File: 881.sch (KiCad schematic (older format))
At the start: 79 parts

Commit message: schematic captured, started layout
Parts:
- SW1: renamed from SW?; footprint (none) -> MyModules:SS-12F45-1P2T-SLIDE
- gave numbers to parts that had none: 78
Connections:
- wire segments 188 -> 128

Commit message: ground stitching, tweaking
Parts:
- R1, R11, R12, R13, R14, R16, R17, R18, R19, R2, R20, R3, R4, R6, R7, R8, R9: value 220 -> 1K
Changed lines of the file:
@@
 P 1775 6675
 F 0 "R1" V 1875 6675 50  0000 C CNN
-F 1 "220" V 1695 6675 50  0000 C CNN
+F 1 "1K" V 1695 6675 50  0000 C CNN
 F 2 "MyModules:SM0603-R-YAGEO" H 1775 6675 60  0001 C CNN
 F 3 "~" H 1775 6675 60  0000 C CNN
@@
 P 1775 7750
 F 0 "R2" V 1875 7750 50  0000 C CNN
-F 1 "220" V 1695 7750 50  0000 C CNN
+F 1 "1K" V 1695 7750 50  0000 C CNN
 F 2 "MyModules:SM0603-R-YAGEO" H 1775 7750 60  0001 C CNN
 F 3 "~" H 1775 7750 60  0000 C CNN
@@
 P 1775 8800
 F 0 "R3" V 1875 8800 50  0000 C CNN
-F 1 "220" V 1695 8800 50  0000 C CNN
+F 1 "1K" V 1695 8800 50  0000 C CNN
 F 2 "MyModules:SM0603-R-YAGEO" H 1775 8800 60  0001 C CNN
 F 3 "~" H 1775 8800 60  0000 C CNN
@@
 P 1775 9875
 F 0 "R4" V 1875 9875 50  0000 C CNN
-F 1 "220" V 1695 9875 50  0000 C CNN
+F 1 "1K" V 1695 9875 50  0000 C CNN
 F 2 "MyModules:SM0603-R-YAGEO" H 1775 9875 60  0001 C CNN
 F 3 "~" H 1775 9875 60  0000 C CNN
@@
 P 3675 6675
 F 0 "R6" V 3775 6675 50  0000 C CNN
-F 1 "220" V 3595 6675 50  0000 C CNN
+F 1 "1K" V 3595 6675 50  0000 C CNN
 F 2 "MyModules:SM0603-R-YAGEO" H 3675 6675 60  0001 C CNN
 F 3 "~" H 3675 6675 60  0000 C CNN
@@
 P 3675 7750
 F 0 "R7" V 3775 7750 50  0000 C CNN
-F 1 "220" V 3595 7750 50  0000 C CNN
+F 1 "1K" V 3595 7750 50  0000 C CNN
 F 2 "MyModules:SM0603-R-YAGEO" H 3675 7750 60  0001 C CNN
 F 3 "~" H 3675 7750 60  0000 C CNN
@@
 P 3675 8800
 F 0 "R8" V 3775 8800 50  0000 C CNN
-F 1 "220" V 3595 8800 50  0000 C CNN
+F 1 "1K" V 3595 8800 50  0000 C CNN
 F 2 "MyModules:SM0603-R-YAGEO" H 3675 8800 60  0001 C CNN
 F 3 "~" H 3675 8800 60  0000 C CNN
@@
 P 3675 9875
 F 0 "R9" V 3775 9875 50  0000 C CNN
-F 1 "220" V 3595 9875 50  0000 C CNN
+F 1 "1K" V 3595 9875 50  0000 C CNN
 F 2 "MyModules:SM0603-R-YAGEO" H 3675 9875 60  0001 C CNN
 F 3 "~" H 3675 9875 60  0000 C CNN
@@
 P 5550 6675
 F 0 "R11" V 5650 6675 50  0000 C CNN
-F 1 "220" V 5470 6675 50  0000 C CNN
+F 1 "1K" V 5470 6675 50  0000 C CNN
 F 2 "MyModules:SM0603-R-YAGEO" H 5550 6675 60  0001 C CNN
 F 3 "~" H 5550 6675 60  0000 C CNN
@@
 P 5550 7750
 F 0 "R12" V 5650 7750 50  0000 C CNN
-F 1 "220" V 5470 7750 50  0000 C CNN
+F 1 "1K" V 5470 7750 50  0000 C CNN
 F 2 "MyModules:SM0603-R-YAGEO" H 5550 7750 60  0001 C CNN
 F 3 "~" H 5550 7750 60  0000 C CNN
@@
 P 5550 8800
 F 0 "R13" V 5650 8800 50  0000 C CNN
-F 1 "220" V 5470 8800 50  0000 C CNN
+F 1 "1K" V 5470 8800 50  0000 C CNN
 F 2 "MyModules:SM0603-R-YAGEO" H 5550 8800 60  0001 C CNN
 F 3 "~" H 5550 8800 60  0000 C CNN
@@
 P 5550 9875
 F 0 "R14" V 5650 9875 50  0000 C CNN
-F 1 "220" V 5470 9875 50  0000 C CNN
+F 1 "1K" V 5470 9875 50  0000 C CNN
 F 2 "MyModules:SM0603-R-YAGEO" H 5550 9875 60  0001 C CNN
 F 3 "~" H 5550 9875 60  0000 C CNN
@@
 P 7775 6675
 F 0 "R16" V 7875 6675 50  0000 C CNN
-F 1 "220" V 7695 6675 50  0000 C CNN
+F 1 "1K" V 7695 6675 50  0000 C CNN
 F 2 "MyModules:SM0603-R-YAGEO" H 7775 6675 60  0001 C CNN
 F 3 "~" H 7775 6675 60  0000 C CNN
@@
 P 7775 7725
 F 0 "R17" V 7875 7725 50  0000 C CNN
-F 1 "220" V 7695 7725 50  0000 C CNN
+F 1 "1K" V 7695 7725 50  0000 C CNN
 F 2 "MyModules:SM0603-R-YAGEO" H 7775 7725 60  0001 C CNN
 F 3 "~" H 7775 7725 60  0000 C CNN
@@
 P 7775 8775
 F 0 "R18" V 7875 8775 50  0000 C CNN
-F 1 "220" V 7695 8775 50  0000 C CNN
+F 1 "1K" V 7695 8775 50  0000 C CNN
 F 2 "MyModules:SM0603-R-YAGEO" H 7775 8775 60  0001 C CNN
 F 3 "~" H 7775 8775 60  0000 C CNN
@@
 P 7775 9850
 F 0 "R19" V 7875 9850 50  0000 C CNN
-F 1 "220" V 7695 9850 50  0000 C CNN
+F 1 "1K" V 7695 9850 50  0000 C CNN
 F 2 "MyModules:SM0603-R-YAGEO" H 7775 9850 60  0001 C CNN
 F 3 "~" H 7775 9850 60  0000 C CNN
@@
 P 10125 6700
 F 0 "R20" V 10225 6700 50  0000 C CNN
-F 1 "220" V 10045 6700 50  0000 C CNN
+F 1 "1K" V 10045 6700 50  0000 C CNN
 F 2 "MyModules:SM0603-R-YAGEO" H 10125 6700 60  0001 C CNN
 F 3 "~" H 10125 6700 60  0000 C CNN

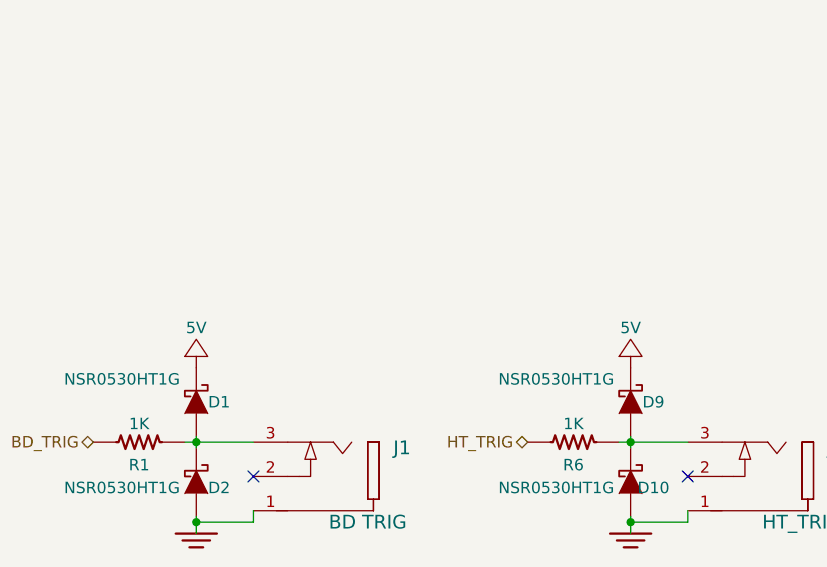
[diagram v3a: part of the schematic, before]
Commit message: notes added, going to turn this into trigger-MIDI converter
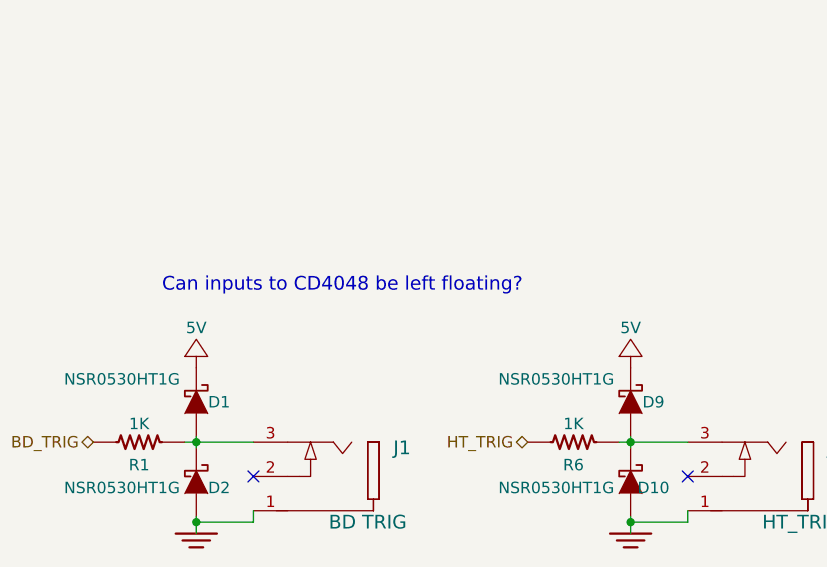
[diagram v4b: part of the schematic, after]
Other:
- note added: "Can inputs to CD4048 be left floating?"
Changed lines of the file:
@@
 	1    0    0    -1
 $EndComp
+Text Notes 1875 6025 0    60   ~ 0
+Can inputs to CD4048 be left floating?
 $EndSCHEMATC

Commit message: first version of 881, obsolete. next commit will begin with new version for connection to 880 TII and DIN EXP
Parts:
- removed C1: 0.01µ, MyModules:SM0603-C-MURATA, symbol C_US
- removed C2, C3: 0.1µ, MyModules:SM0603-C-MURATA, symbol C_US
- removed D1, D10, D11, D12, D13, D14, D15, D16, D17, D18, D19, D2, D20, D21, D22, D23, D24, D25, D26, D3, D4, D5, D6, D7, D8, D9: NSR0530HT1G, MyModules:SOD323-C1A2, symbol D_Schottky
- removed R1, R11, R12, R13, R14, R16, R2, R3, R4, R6, R7, R8, R9: 1K, MyModules:SM0603-R-YAGEO, symbol R_US
- removed R5: 22, MyModules:SM0603-R-YAGEO, symbol R_US
- removed SW1: SPDT, MyModules:SS-12F45-1P2T-SLIDE, symbol SPDT
- removed U1, U2: CD4048B, Housings_SSOP:TSSOP-16_4.4x5mm_Pitch0.65mm, symbol CD4048B
- removed X1: SYNC24 OUT, MyModules:SD-50BV-5DIN, symbol MIDI_DIN
- added C?: 1μ, MyModules:SM0603-C-JRL, symbol C_US
- added C? (x2): 47µ, Capacitors_SMD:c_elec_4x5.3, symbol CP_US
- added C? (x12): 0.1μ, MyModules:SM0603-C-JRL, symbol C_US
- added C? (x2): 24p, MyModules:SM0603-C-JRL, symbol C_US
- added C? (x5): 0.1µ, MyModules:SM0603-C-JRL, symbol C_US
- added D? (x2): SMB, MyModules:SMB-1C2A, symbol D
- added D? (x4): NSR0530HT1G, MyModules:SOD323-C1A2, symbol D_Schottky
- added D?: LED 7, MyModules:3MM-LED-C1A2, symbol LED
- added D?: LED 8, MyModules:3MM-LED-C1A2, symbol LED
- added D?: LED 5, MyModules:3MM-LED-C1A2, symbol LED
- added D?: LED 6, MyModules:3MM-LED-C1A2, symbol LED
- added D?: LED 3, MyModules:3MM-LED-C1A2, symbol LED
- added D?: LED 4, MyModules:3MM-LED-C1A2, symbol LED
- added D?: LED 1, MyModules:3MM-LED-C1A2, symbol LED
- added D?: LED 2, MyModules:3MM-LED-C1A2, symbol LED
- added F? (x2): FUSE, MyModules:SM0805-HAND, symbol FUSE
- added IC?: ATMEGA328PB, Housings_QFP:TQFP-32_7x7mm_Pitch0.8mm, symbol ATMEGA328PB
- added J?: ASSIGN 1 IN, MyModules:PJ-301B-JACK-SLOTS, symbol JACK_MONO_SW
- added J?: ASSIGN 2 IN, MyModules:PJ-301B-JACK-SLOTS, symbol JACK_MONO_SW
- added J?: SYNC IN, MyModules:PJ-301B-JACK-SLOTS, symbol JACK_MONO_SW
- added L? (x2): BEAD, MyModules:SM0805-HAND, symbol INDUCTOR
- added L?: 10µ, MyModules:SM0805-HAND, symbol INDUCTOR
- added P?: CONN_02X05, Pin_Headers:Pin_Header_Straight_2x05, symbol CONN_02X05
- added Q?: C945, MyModules:SOT23-132-JRL, symbol C945
- added Q? (x15): MMBT3904, MyModules:SOT23-132-JRL, symbol C945
- added R? (x2): 1K, MyModules:SM0603-R-JRL, symbol R_US
- added R? (x2): 1K, MyModules:SM0603-R-YAGEO, symbol R_US
- added R? (x17): 10K, MyModules:SM0603-R-JRL, symbol R_US
- added R? (x2): 47K, MyModules:SM0603-R-JRL, symbol R_US
- added R?: 4.7K, MyModules:SM0603-R-JRL, symbol R_US
- added R? (x8): 3.3K, MyModules:SM0603-R-YAGEO, symbol R_US
- added R? (x15): 100K, MyModules:SM0603-R-JRL, symbol R_US
- added R? (x15): 1meg, MyModules:SM0603-R-JRL, symbol R_US
- added SW?: SWITCH A, MyModules:B3F-1050-OMRON, symbol TACT_SWITCH
- added SW?: SWITCH B, MyModules:B3F-1050-OMRON, symbol TACT_SWITCH
- added TP? (x2): CONN_1, MyModules:TEST_POINT_LOOP_4592, symbol CONN_1
- added U?: MCP1703, TO_SOT_Packages_SMD:SOT-223, symbol MCP1703
- added U? (x2): 74HC165, Housings_SSOP:TSSOP-16_4.4x5mm_Pitch0.65mm, symbol 74HC165
- added Y?: 16MHz, synth:403-XTAL-4-SMD, symbol Crystal
- renumbered J13 to J?
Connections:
- net labels added: +12V, -12V, ASSIGN_1, ASSIGN_2, BD, CB, CH, CP, CY, GND_R, HT, ISP_MISO, ISP_MOSI, ISP_SCK, LED_LATCH, MA, OH, RS, SD, SPI_MISO, SPI_MOSI, SPI_SCK, START/STOP, SWITCH_LATCH, SYNC_IN, SYNC_LED_R, SYNC_LED_Y, TAP, TEMPO, TRIG_OUT_1, TRIG_OUT_2, UART_RX, ~RESET, ~SPI_EN
- wire segments 128 -> 315
- no-connect marks 24 -> 12
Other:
- note added: "Need to add protection/\nrectification here?\n"
- note added: "PINPOUT FIXED\nDOUBLE CHECK"
- note removed: "Can inputs to CD4048 be left floating?"
- moved on the sheet: D27, D28, D29, D30, D31, D32, J1, J10, J11, J12, J14, J15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

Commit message: schematic and footprint almost complete. spi clock or run-stop line for TII active indication still debatable, but leaning towards SPI SCK for LED indication
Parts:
- removed C?: 1μ, MyModules:SM0603-C-JRL, symbol C_US
- removed C? (x2): 47µ, Capacitors_SMD:c_elec_4x5.3, symbol CP_US
- removed C? (x12): 0.1μ, MyModules:SM0603-C-JRL, symbol C_US
- removed C? (x2): 24p, MyModules:SM0603-C-JRL, symbol C_US
- removed C? (x5): 0.1µ, MyModules:SM0603-C-JRL, symbol C_US
- removed D27, D28, D29, D30, D31, D32, D? (x4): NSR0530HT1G, MyModules:SOD323-C1A2, symbol D_Schottky
- removed D? (x2): SMB, MyModules:SMB-1C2A, symbol D
- removed D?: LED 7, MyModules:3MM-LED-C1A2, symbol LED
- removed D?: LED 8, MyModules:3MM-LED-C1A2, symbol LED
- removed D?: LED 5, MyModules:3MM-LED-C1A2, symbol LED
- removed D?: LED 6, MyModules:3MM-LED-C1A2, symbol LED
- removed D?: LED 3, MyModules:3MM-LED-C1A2, symbol LED
- removed D?: LED 4, MyModules:3MM-LED-C1A2, symbol LED
- removed D?: LED 1, MyModules:3MM-LED-C1A2, symbol LED
- removed D?: LED 2, MyModules:3MM-LED-C1A2, symbol LED
- removed F? (x2): FUSE, MyModules:SM0805-HAND, symbol FUSE
- removed IC?: ATMEGA328PB, Housings_QFP:TQFP-32_7x7mm_Pitch0.8mm, symbol ATMEGA328PB
- removed J17: ACCENT OUT, MyModules:PJ-301B-JACK-SLOTS, symbol JACK_MONO_SW
- removed J?: ACCENT IN, MyModules:PJ-301B-JACK-SLOTS, symbol JACK_MONO_SW
- removed J?: ASSIGN 1 IN, MyModules:PJ-301B-JACK-SLOTS, symbol JACK_MONO_SW
- removed J?: ASSIGN 2 IN, MyModules:PJ-301B-JACK-SLOTS, symbol JACK_MONO_SW
- removed J?: SYNC IN, MyModules:PJ-301B-JACK-SLOTS, symbol JACK_MONO_SW
- removed L? (x2): BEAD, MyModules:SM0805-HAND, symbol INDUCTOR
- removed L?: 10µ, MyModules:SM0805-HAND, symbol INDUCTOR
- removed P2: CONN_02X10, w_conn_strip:vasch_strip_10x2, symbol CONN_02X10
- removed P?: CONN_02X05, Pin_Headers:Pin_Header_Straight_2x05, symbol CONN_02X05
- removed Q?: C945, MyModules:SOT23-132-JRL, symbol C945
- removed Q? (x15): MMBT3904, MyModules:SOT23-132-JRL, symbol C945
- removed R? (x2): 1K, MyModules:SM0603-R-JRL, symbol R_US
- removed R? (x2): 1K, MyModules:SM0603-R-YAGEO, symbol R_US
- removed R? (x17): 10K, MyModules:SM0603-R-JRL, symbol R_US
- removed R? (x2): 47K, MyModules:SM0603-R-JRL, symbol R_US
- removed R?: 4.7K, MyModules:SM0603-R-JRL, symbol R_US
- removed R? (x8): 3.3K, MyModules:SM0603-R-YAGEO, symbol R_US
- removed R? (x15): 100K, MyModules:SM0603-R-JRL, symbol R_US
- removed R? (x15): 1meg, MyModules:SM0603-R-JRL, symbol R_US
- removed SW?: SWITCH A, MyModules:B3F-1050-OMRON, symbol TACT_SWITCH
- removed SW?: SWITCH B, MyModules:B3F-1050-OMRON, symbol TACT_SWITCH
- removed TP? (x2): CONN_1, MyModules:TEST_POINT_LOOP_4592, symbol CONN_1
- removed U?: MCP1703, TO_SOT_Packages_SMD:SOT-223, symbol MCP1703
- removed U? (x2): 74HC165, Housings_SSOP:TSSOP-16_4.4x5mm_Pitch0.65mm, symbol 74HC165
- removed Y?: 16MHz, synth:403-XTAL-4-SMD, symbol Crystal
- added C1: 0.01µ, MyModules:SM0603-C-MURATA, symbol C_US
- added C15: 1µ, Capacitors_SMD:C_0805, symbol C_US
- added C19, C2, C20, C3: 0.1µ, MyModules:SM0603-C-MURATA, symbol C_US
- added C?: 1n, MyModules:SM0603-C-MURATA, symbol C_US
- added D1, D2, D3, D4: B5819W, Diodes_SMD:D_SOD-123, symbol D_Schottky
- added D10, D11, D12, D13, D14, D15, D16, D6, D7, D8, D9: 1N4148, MyModules:SOD323-C1A2, symbol D
- added D5: 1N4148, Diodes_SMD:D_SOD-323F, symbol D
- added D? (x2): LED, symbol LED
- added ISP1: CONN_02X03, w_conn_strip:vasch_strip_3x2, symbol CONN_02X03
- added J13: CB IN, MyModules:PJ-301B-JACK-SLOTS, symbol JACK_MONO_SW
- added Q1, Q10, Q11, Q12, Q2, Q3, Q4, Q5, Q6, Q7, Q8, Q9, Q? (x3): MMBT3904, MyModules:SOT23-132-JRL, symbol C945
- added Q?: MMBT3906, SOT-23, symbol MMBT3906
- added R1, R3: 220, MyModules:SM0603-R-YAGEO, symbol R_US
- added R11, R12, R13, R21, R22, R23, R24, R25, R30, R31, R32, R33, R34, R35, R36, R37, R43, R6, R7, R8, R9, R? (x3): 100K, MyModules:SM0603-R-YAGEO, symbol R_US
- added R14, R16, R26, R27, R28, R29, R38, R39, R40, R41, R? (x3): 10K, MyModules:SM0603-R-YAGEO, symbol R_US
- added R2: 22, MyModules:SM0603-R-YAGEO, symbol R_US
- added R4, R5, R? (x3): 1K, MyModules:SM0603-R-YAGEO, symbol R_US
- added R42, R44, R45: 47K, MyModules:SM0603-R-YAGEO, symbol R_US
- added TP1, TP2: CONN_1, MyModules:TEST_POINT_LOOP_4592, symbol CONN_1
- added U1, U2: 74HC165, Housings_SOIC:SOIC-16_3.9x9.9mm_Pitch1.27mm, symbol 74HC165
- added U7: 74HCT1G125GV, TO_SOT_Packages_SMD:SOT-353_SC-70-5, symbol 74HC1G125
- added X1: MIDI OUT, MyModules:SD-50BV-5DIN, symbol MIDI_DIN
- J1: value BD TRIG -> RUN/STOP
- J10: value CY TRIG -> RS IN
- J11: value OH TRIG -> CP IN
- J12: value CH_TRIG -> MA IN
- J14: value RUN/STOP -> CY IN
- J15: value RESET -> OH IN
- J16: value CLOCK OUT -> CH IN
- J2: value SD TRIG -> SYNC24 CLK
- J3: value LT TRIG -> ASSIGN 1
- J4: value MT TRIG -> ASSIGN 2
- J5: value HT_TRIG -> BD IN
- J6: value RS TRIG -> SD IN
- J7: value CP_TRIG -> LT IN
- J8: value MA_TRIG -> MT IN
- J9: value CB TRIG -> HT IN
- P1: footprint w_conn_strip:vasch_strip_3x2 -> w_conn_strip:vasch_strip_4x2
- R10: value 220 -> 100K
- R15: value 220 -> 10K
- R17: value 1K -> 10K
- R18, R19, R20: value 1K -> 100K
- X2: value MIDI OUT -> SYNC24
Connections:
- net +5V: now also R15.1, R17.1, C15.1, C19.1, C2.1, C20.1, C3.1, D1.1 (K), D3.1 (K), ISP1.2 (P2), R14.1, R16.1, R26.1, R27.1, R28.1, R29.1, R3.2, R38.1, R39.1, R40.1, R41.1, R44.1, R?.1, R?.1, R?.1, R?.1, R?.2, U1.16 (VCC), U2.16 (VCC), U7.6 (VCC); no longer R15.2
- net BD: now also Q1.3 (C), R14.2, U1.11 (D0)
- net CB: now also Q9.3 (C), R38.2, U2.11 (D0)
- net CH: now also Q12.3 (C), R41.2, U2.14 (D3)
- net CP: now also Q7.3 (C), R28.2, U1.5 (D6)
- net CY: now also Q10.3 (C), R39.2, U2.12 (D1)
- net DIN_FILL: now also R43.1, R5.2
- net DIN_RESET: now also R4.2, R42.1
- net DIN_RUN_STOP: now also J1.3, X2.1, R?.1, U7.1 (~OE)
- net DIN_TEMPO_CLK: now also J2.3, X2.3
- net GND: now also TP2.1; no longer J1.2, J10.1, J10.2, J11.1, J11.2, J12.1, J12.2, J14.1, J15.1, J16.1, J2.1, J2.2, J4.1, J4.2, J5.1, J5.2, J6.1, J6.2, J7.1, J7.2, J8.1, J8.2, J9.1, J9.2, P1.3 (P3), X2.2
- net HT: now also Q5.3 (C), R26.2, U1.3 (D4)
- net ISP_MISO: now also ISP1.1 (P1), R44.2, R45.1, TP1.1, U7.4 (Y)
- net ISP_MOSI: now also ISP1.4 (P4), U1.1 (~PL), U2.1 (~PL)
- net ISP_SCK: now also ISP1.3 (P3), R?.2, U1.2 (SCK), U2.2 (SCK)
- net MA: now also Q8.3 (C), R29.2, U1.6 (D7)
- net OH: now also Q11.3 (C), R40.2, U2.13 (D2)
- net RS: now also Q6.3 (C), R27.2, U1.4 (D5)
- net SD: now also R15.2, Q2.3 (C), U1.12 (D1)
- net UART_TX: now also R1.2; no longer R10.2
- net GNDD: now reaches J1.1
- net GNDD: now also J10.1, J10.2, J11.1, J11.2, J12.1, J12.2, J14.1, J14.2, J15.1, J15.2, J16.1, J16.2, J2.1, J3.1, J4.1, J5.1, J5.2, J6.1, J6.2, J7.1, J7.2, J8.1, J8.2, J9.1, J9.2, P1.3 (P3), R10.2, C1.2, C15.2, C19.2, C2.2, C20.2, C3.2, C?.2, D10.2 (A), D11.2 (A), D12.2 (A), D13.2 (A), D14.2 (A), D15.2 (A), D16.2 (A), D2.2 (A), D4.2 (A), D5.2 (A), D6.2 (A), D7.2 (A), D8.2 (A), D9.2 (A), ISP1.6 (P6), J13.1, J13.2, Q1.2 (E), Q10.2 (E), Q11.2 (E), Q12.2 (E), Q2.2 (E), Q3.2 (E), Q4.2 (E), Q5.2 (E), Q6.2 (E), Q7.2 (E), Q8.2 (E), Q9.2 (E), Q?.2 (E), Q?.2 (E), Q?.2 (E), Q?.3 (C), R11.2, R12.2, R13.2, R2.1, R22.2, R23.2, R24.2, R25.2, R34.2, R35.2, R36.2, R37.2, R42.2, R43.2, R45.2, U1.15 (~CE), U1.8 (GND), U2.15 (~CE), U2.3 (D4), U2.4 (D5), U2.5 (D6), U2.6 (D7), U2.8 (GND), U7.3 (GNDD), X1.2
- net at X2.4: no longer R15.1
- net at X2.5: no longer R10.1
- net at J3.3: now also D1.2 (A), D2.1 (K), R4.1
- net at J4.3: now also D3.2 (A), D4.1 (K), R5.1
- net at J5.3: now also R6.1
- net at J6.3: now also R7.1
- net at J7.3: now also R8.1
- net at J8.3: now also R9.1
- net at J9.3: now also R18.1
- net at J10.3: now also R19.1
- net at J11.3: now also R20.1
- net at J12.3: now also R21.1
- net at J14.3: now also R31.1; no longer R17.1
- net MT: now reaches R17.2
- net MT: now also Q4.3 (C), U1.14 (D3)
- net at J15.3: now also R32.1; no longer R18.1
- net at R18.2: now also D9.1 (K), Q5.1 (B), R22.1
- net at J16.3: now also R33.1; no longer R19.1
- net at R19.2: now also D10.1 (K), Q6.1 (B), R23.1
- net at R20.2: now also D11.1 (K), Q7.1 (B), R24.1
- new net: C1.1, R2.2, X2.2
- new net: D5.1 (K), Q1.1 (B), R10.1, R6.2
- new net: U1.9 (Q7), U2.10 (SER)
- new net: U2.9 (Q7), U7.2 (A)
- new net: R3.1, X1.4
- new net: R1.1, X1.5
- new net: D6.1 (K), Q2.1 (B), R11.1, R7.2
- new net: D7.1 (K), Q3.1 (B), R12.1, R8.2
- new net: D8.1 (K), Q4.1 (B), R13.1, R9.2
- new net: D12.1 (K), Q8.1 (B), R21.2, R25.1
- new net: J13.3, R30.1
- new net: D13.1 (K), Q9.1 (B), R30.2, R34.1
- new net: D14.1 (K), Q10.1 (B), R31.2, R35.1
- new net: D15.1 (K), Q11.1 (B), R32.2, R36.1
- new net: D16.1 (K), Q12.1 (B), R33.2, R37.1
- new net: Q?.1 (B), R?.2, R?.2
- new net: Q?.1 (B), R?.1 (x2)
- new net: D?.1 (K), Q?.3 (C)
- new net: D?.2 (A), R?.2 (x2)
- new net: Q?.3 (C), R?.1, R?.2
- new net: Q?.3 (C), R?.2, R?.2
- new net: D?.1 (K), Q?.2 (E)
- new net: C?.1, Q?.1 (B), R?.1
- new net LT: Q3.3 (C), R16.2, U1.13 (D2)
- no-connect marks 12 -> 14
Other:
- note added: "GND through 22R and\ndecoupling C taken\nfrom TR-606 schematic"
- note added: "Input protection is on\nmain 880 board"
- note added: "PULL UP HERE"
- note added: "PULL UP OR DOWN HERE?"
- note added: "SYNC24"
- note added: "TSOP-5-SC74A-SOT-753"
- note added: "USE ISP_MOSI as LATCH"
- note removed: "'881' TRIGGER EXPANDER FOR 880"
- note removed: "DIN HEADER"
- note removed: "Need to add protection/\nrectification here?\n"
- note removed: "PINPOUT FIXED\nDOUBLE CHECK"
- note removed: "SYSTEM80 INC."
- note removed: "TRIGGER \nHEADER"

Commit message: first route
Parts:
- removed D?: LED, symbol LED
- removed Q? (x2): MMBT3904, MyModules:SOT23-132-JRL, symbol C945
- removed R? (x2): 100K, MyModules:SM0603-R-YAGEO, symbol R_US
- removed R?: 1K, MyModules:SM0603-R-YAGEO, symbol R_US
- removed R? (x2): 10K, MyModules:SM0603-R-YAGEO, symbol R_US
- removed U7: 74HCT1G125GV, TO_SOT_Packages_SMD:SOT-353_SC-70-5, symbol 74HC1G125
- added D18: LED, LEDs:LED_D3.0mm, symbol LED
- added U7: 74AHCT1G125GW, TO_SOT_Packages_SMD:SOT-353_SC-70-5, symbol 74AHCT1G125GW
- D17: renamed from D?; footprint (none) -> LEDs:LED_0805; JLC (none) -> C84256
- gave numbers to parts that had none: 7
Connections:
- net +5V: now also U7.5 (VCC)
- net DIN_RUN_STOP: now also U7.1 (~OE)
- net GNDD: now also U7.3 (GNDD)
- net ISP_MISO: now also U7.4 (Y)
- net at U2.9 (Q7): now also U7.2 (A)
- net at D17.1 (K), Q14.2 (E): now also D18.1 (K)
- net at D17.2 (A), R49.2: now also D18.2 (A)
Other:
- moved on the sheet: C4, D17, Q13, Q14, R46, R47, R48, R49
